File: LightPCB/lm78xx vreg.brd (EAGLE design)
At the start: 33.3 x 30.5 mm, 15 parts, among them IC1 7805TV, J1 +18v

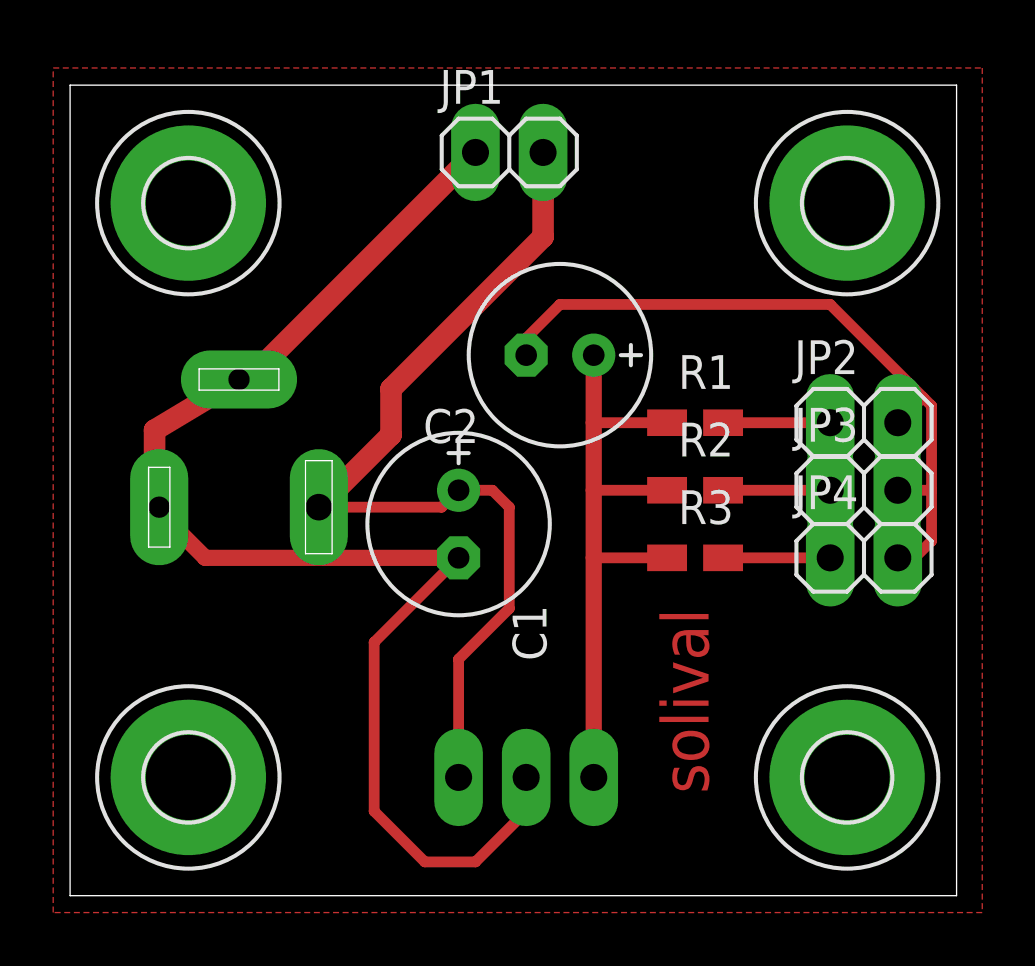
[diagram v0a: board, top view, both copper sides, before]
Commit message: Changed DRC for light PCB
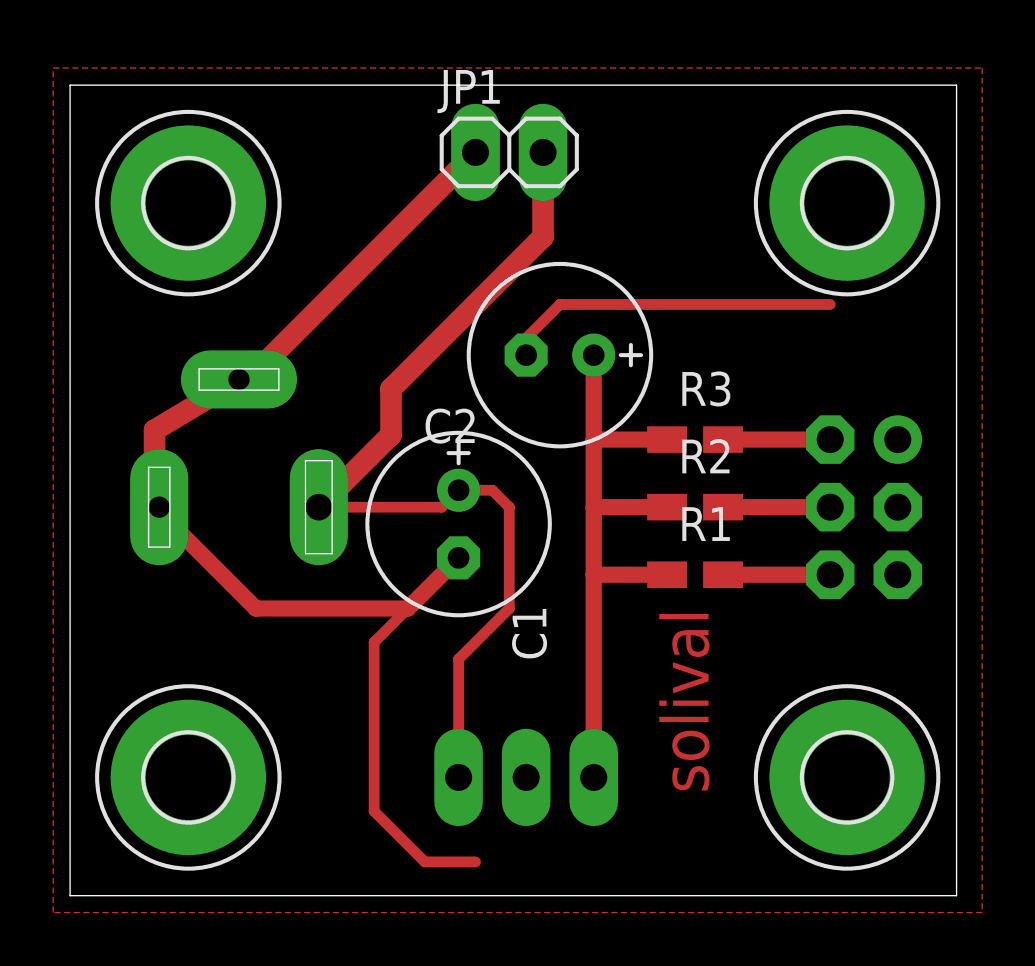
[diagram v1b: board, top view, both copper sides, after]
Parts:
- removed JP2: LED1, pinhead:1X02
- removed JP3: LED2, pinhead:1X02
- removed JP4: LED3, pinhead:1X02
- added SV1: (no value), con-lstb:MA03-2
- moved R1 5.72 mm to (24.1, 12.1)
- moved R3 4.45 mm to (24.1, 17.1)
- moved R2 0.63 mm to (24.1, 14.6)
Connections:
- removed net N$6: JP2.1, R1.2
- removed net N$7: JP3.1, R2.2
- removed net N$8: JP4.1, R3.2
- new net N$3: R2.2, SV1.4
- new net N$4: R1.2, SV1.6
- new net N$5: R3.2, SV1.2
- net GND: now also SV1.1, SV1.3, SV1.5; no longer JP2.2, JP3.2, JP4.2
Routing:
- net GND: track 77.9 -> 62.1 mm
- net N$8: track 4.03 -> 0.00 mm
- net N$7: track 4.03 -> 0.00 mm
- net N$6: track 4.03 -> 0.00 mm
- net N$5: track 0.00 -> 4.03 mm
- net N$4: track 0.00 -> 4.03 mm
- net N$3: track 0.00 -> 4.03 mm
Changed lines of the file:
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@@
 <param name="rlMinMicroViaInner" value="4mil"/>
 <param name="rlMaxMicroViaInner" value="20mil"/>
-<param name="psTop" value="2"/>
-<param name="psBottom" value="2"/>
+<param name="psTop" value="-1"/>
+<param name="psBottom" value="-1"/>
 <param name="psFirst" value="0"/>
 <param name="psElongationLong" value="100"/>
@@
 </element>
 <element name="JP1" library="pinhead" package="1X02" value="M_OUT" x="17.145" y="27.94"/>
-<element name="JP2" library="pinhead" package="1X02" value="LED1" x="30.48" y="17.78"/>
-<element name="JP3" library="pinhead" package="1X02" value="LED2" x="30.48" y="15.24"/>
-<element name="JP4" library="pinhead" package="1X02" value="LED3" x="30.48" y="12.7"/>
-<element name="R1" library="rcl" package="R0805W" value="100" x="24.13" y="17.78"/>
-<element name="R2" library="rcl" package="R0805W" value="100" x="24.13" y="15.24"/>
-<element name="R3" library="rcl" package="R0805W" value="100" x="24.13" y="12.7"/>
+<element name="R1" library="rcl" package="R0805W" value="100" x="24.13" y="12.065"/>
+<element name="R2" library="rcl" package="R0805W" value="100" x="24.13" y="14.605"/>
+<element name="R3" library="rcl" package="R0805W" value="100" x="24.13" y="17.145"/>
 <element name="H5" library="holes" package="3,2-PAD" value="MOUNT-PAD-ROUND3.2" x="5.08" y="26.035"/>
 <element name="H6" library="holes" package="3,2-PAD" value="MOUNT-PAD-ROUND3.2" x="29.845" y="26.035"/>
 <element name="H7" library="holes" package="3,2-PAD" value="MOUNT-PAD-ROUND3.2" x="29.845" y="4.445"/>
 <element name="H8" library="holes" package="3,2-PAD" value="MOUNT-PAD-ROUND3.2" x="5.08" y="4.445"/>
+<element name="SV1" library="con-lstb" package="MA03-2" value="" x="30.48" y="14.605" rot="MR270">
+<attribute name="OC_NEWARK" value="unknown" x="30.48" y="14.605" size="1.778" layer="28" rot="MR270" display="off"/>
+<attribute name="MPN" value="" x="30.48" y="14.605" size="1.778" layer="28" rot="MR270" display="off"/>
+<attribute name="MF" value="" x="30.48" y="14.605" size="1.778" layer="28" rot="MR270" display="off"/>
+<attribute name="OC_FARNELL" value="unknown" x="30.48" y="14.605" size="1.778" layer="28" rot="MR270" display="off"/>
+</element>
 </elements>
 <signals>
@@
 <contactref element="R2" pad="1"/>
 <contactref element="R3" pad="1"/>
-<wire x1="23.0775" y1="12.7" x2="20.32" y2="12.7" width="0.4064" layer="1"/>
-<wire x1="20.32" y1="15.24" x2="20.32" y2="17.78" width="0.6096" layer="1"/>
-<wire x1="20.32" y1="17.78" x2="20.32" y2="20.32" width="0.6096" layer="1"/>
-<wire x1="20.32" y1="4.445" x2="20.32" y2="12.7" width="0.6096" layer="1"/>
-<wire x1="20.32" y1="12.7" x2="20.32" y2="15.24" width="0.6096" layer="1"/>
-<wire x1="23.0775" y1="15.24" x2="20.32" y2="15.24" width="0.4064" layer="1"/>
-<wire x1="23.0775" y1="17.78" x2="20.32" y2="17.78" width="0.4064" layer="1"/>
+<wire x1="20.32" y1="4.445" x2="20.32" y2="12.065" width="0.6096" layer="1"/>
+<wire x1="20.32" y1="12.065" x2="20.32" y2="14.605" width="0.6096" layer="1"/>
+<wire x1="20.32" y1="14.605" x2="20.32" y2="17.145" width="0.6096" layer="1"/>
+<wire x1="20.32" y1="17.145" x2="20.32" y2="20.32" width="0.6096" layer="1"/>
+<wire x1="23.0775" y1="12.065" x2="20.32" y2="12.065" width="0.6096" layer="1"/>
+<wire x1="23.0775" y1="14.605" x2="20.32" y2="14.605" width="0.6096" layer="1"/>
+<wire x1="23.0775" y1="17.145" x2="20.32" y2="17.145" width="0.6096" layer="1"/>
 </signal>
 <signal name="GND">
@@
 <contactref element="J1" pad="2"/>
 <contactref element="JP1" pad="1"/>
-<contactref element="JP2" pad="2"/>
-<contactref element="JP3" pad="2"/>
-<contactref element="JP4" pad="2"/>
 <polygon width="0.4064" layer="1" isolate="0.6096">
 <vertex x="0" y="31.115"/>
@@
 <contactref element="H7" pad="B3,2"/>
 <contactref element="H8" pad="B3,2"/>
-<wire x1="15.24" y1="12.7" x2="5.715" y2="12.7" width="0.6096" layer="1"/>
-<wire x1="5.715" y1="12.7" x2="3.81" y2="14.605" width="0.6096" layer="1"/>
 <wire x1="3.81" y1="14.605" x2="3.81" y2="17.5" width="0.8128" layer="1"/>
 <wire x1="3.81" y1="17.5" x2="6.985" y2="19.405" width="0.8128" layer="1"/>
 <wire x1="17.78" y1="4.445" x2="17.78" y2="3.175" width="0.4064" layer="1"/>
-<wire x1="17.78" y1="3.175" x2="15.875" y2="1.27" width="0.4064" layer="1"/>
 <wire x1="15.875" y1="1.27" x2="13.97" y2="1.27" width="0.4064" layer="1"/>
 <wire x1="13.97" y1="1.27" x2="12.065" y2="3.175" width="0.4064" layer="1"/>
@@
 <wire x1="12.065" y1="9.525" x2="15.24" y2="12.7" width="0.4064" layer="1"/>
 <wire x1="6.985" y1="19.405" x2="7.34" y2="19.405" width="0.8128" layer="1"/>
-<wire x1="31.75" y1="12.7" x2="32.385" y2="12.7" width="0.4064" layer="1"/>
-<wire x1="32.385" y1="12.7" x2="33.02" y2="13.335" width="0.4064" layer="1"/>
-<wire x1="33.02" y1="13.335" x2="33.02" y2="15.24" width="0.4064" layer="1"/>
-<wire x1="33.02" y1="15.24" x2="33.02" y2="18.415" width="0.4064" layer="1"/>
-<wire x1="33.02" y1="18.415" x2="32.7025" y2="18.7325" width="0.4064" layer="1"/>
-<wire x1="32.7025" y1="18.7325" x2="29.21" y2="22.225" width="0.4064" layer="1"/>
-<wire x1="31.75" y1="15.24" x2="33.02" y2="15.24" width="0.4064" layer="1"/>
-<wire x1="31.75" y1="17.78" x2="32.7025" y2="18.7325" width="0.4064" layer="1"/>
 <wire x1="17.78" y1="20.32" x2="17.78" y2="20.955" width="0.4064" layer="1"/>
 <wire x1="17.78" y1="20.955" x2="19.05" y2="22.225" width="0.4064" layer="1"/>
 <wire x1="19.05" y1="22.225" x2="29.21" y2="22.225" width="0.4064" layer="1"/>
 <wire x1="7.34" y1="19.405" x2="15.875" y2="27.94" width="0.8128" layer="1"/>
-</signal>
-<signal name="N$6">
+<wire x1="3.81" y1="14.605" x2="7.62" y2="10.795" width="0.6096" layer="1"/>
+<wire x1="7.62" y1="10.795" x2="13.335" y2="10.795" width="0.6096" layer="1"/>
+<wire x1="13.335" y1="10.795" x2="15.24" y2="12.7" width="0.6096" layer="1"/>
+<contactref element="SV1" pad="5"/>
+<contactref element="SV1" pad="3"/>
+<contactref element="SV1" pad="1"/>
+</signal>
+<signal name="N$3">
+<contactref element="R2" pad="2"/>
+<contactref element="SV1" pad="4"/>
+<wire x1="29.21" y1="14.605" x2="25.1825" y2="14.605" width="0.6096" layer="1"/>
+</signal>
+<signal name="N$4">
 <contactref element="R1" pad="2"/>
-<contactref element="JP2" pad="1"/>
-<wire x1="25.1825" y1="17.78" x2="29.21" y2="17.78" width="0.4064" layer="1"/>
-</signal>
-<signal name="N$7">
-<contactref element="JP3" pad="1"/>
-<contactref element="R2" pad="2"/>
-<wire x1="25.1825" y1="15.24" x2="29.21" y2="15.24" width="0.4064" layer="1"/>
-</signal>
-<signal name="N$8">
-<contactref element="JP4" pad="1"/>
+<contactref element="SV1" pad="6"/>
+<wire x1="29.21" y1="12.065" x2="25.1825" y2="12.065" width="0.6096" layer="1"/>
+</signal>
+<signal name="N$5">
 <contactref element="R3" pad="2"/>
-<wire x1="25.1825" y1="12.7" x2="29.21" y2="12.7" width="0.4064" layer="1"/>
+<contactref element="SV1" pad="2"/>
+<wire x1="29.21" y1="17.145" x2="25.1825" y2="17.145" width="0.6096" layer="1"/>
 </signal>
 </signals>
